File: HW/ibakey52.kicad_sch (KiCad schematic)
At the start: 55 parts, among them J1 AudioJack4, U1 Nice!Nano

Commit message: Renaming project
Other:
- sheet Keys: file ibakey54-keys.kicad_sch -> ibakey52-keys.kicad_sch

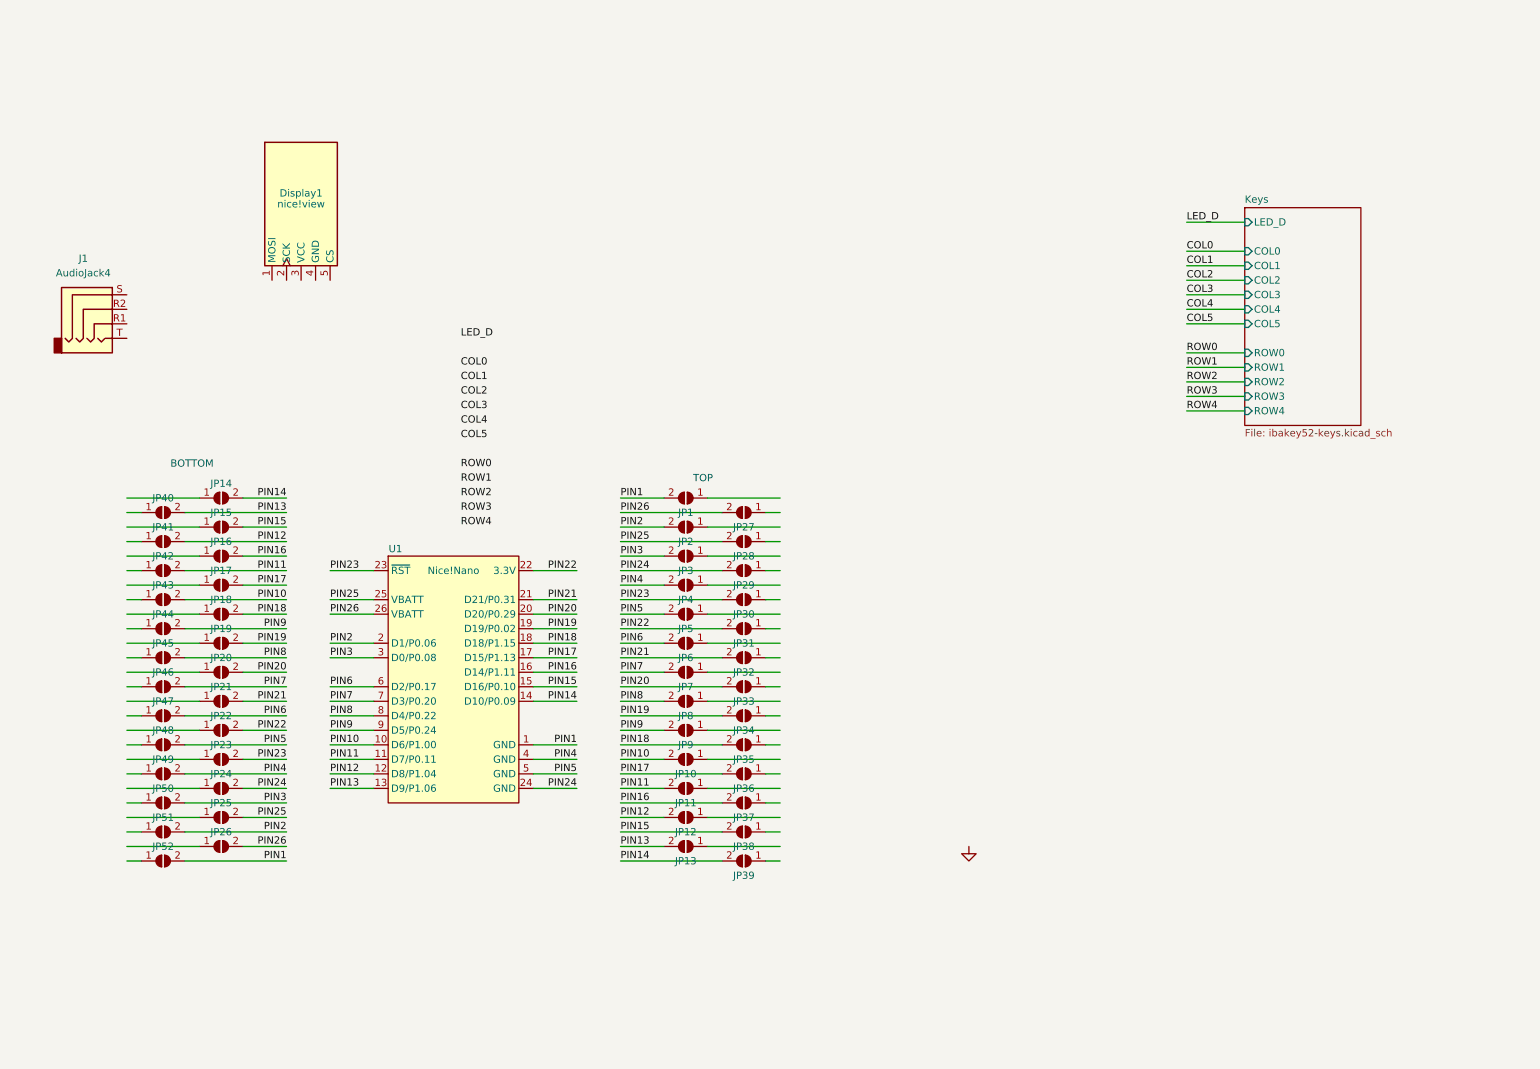
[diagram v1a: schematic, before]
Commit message: matrix routed
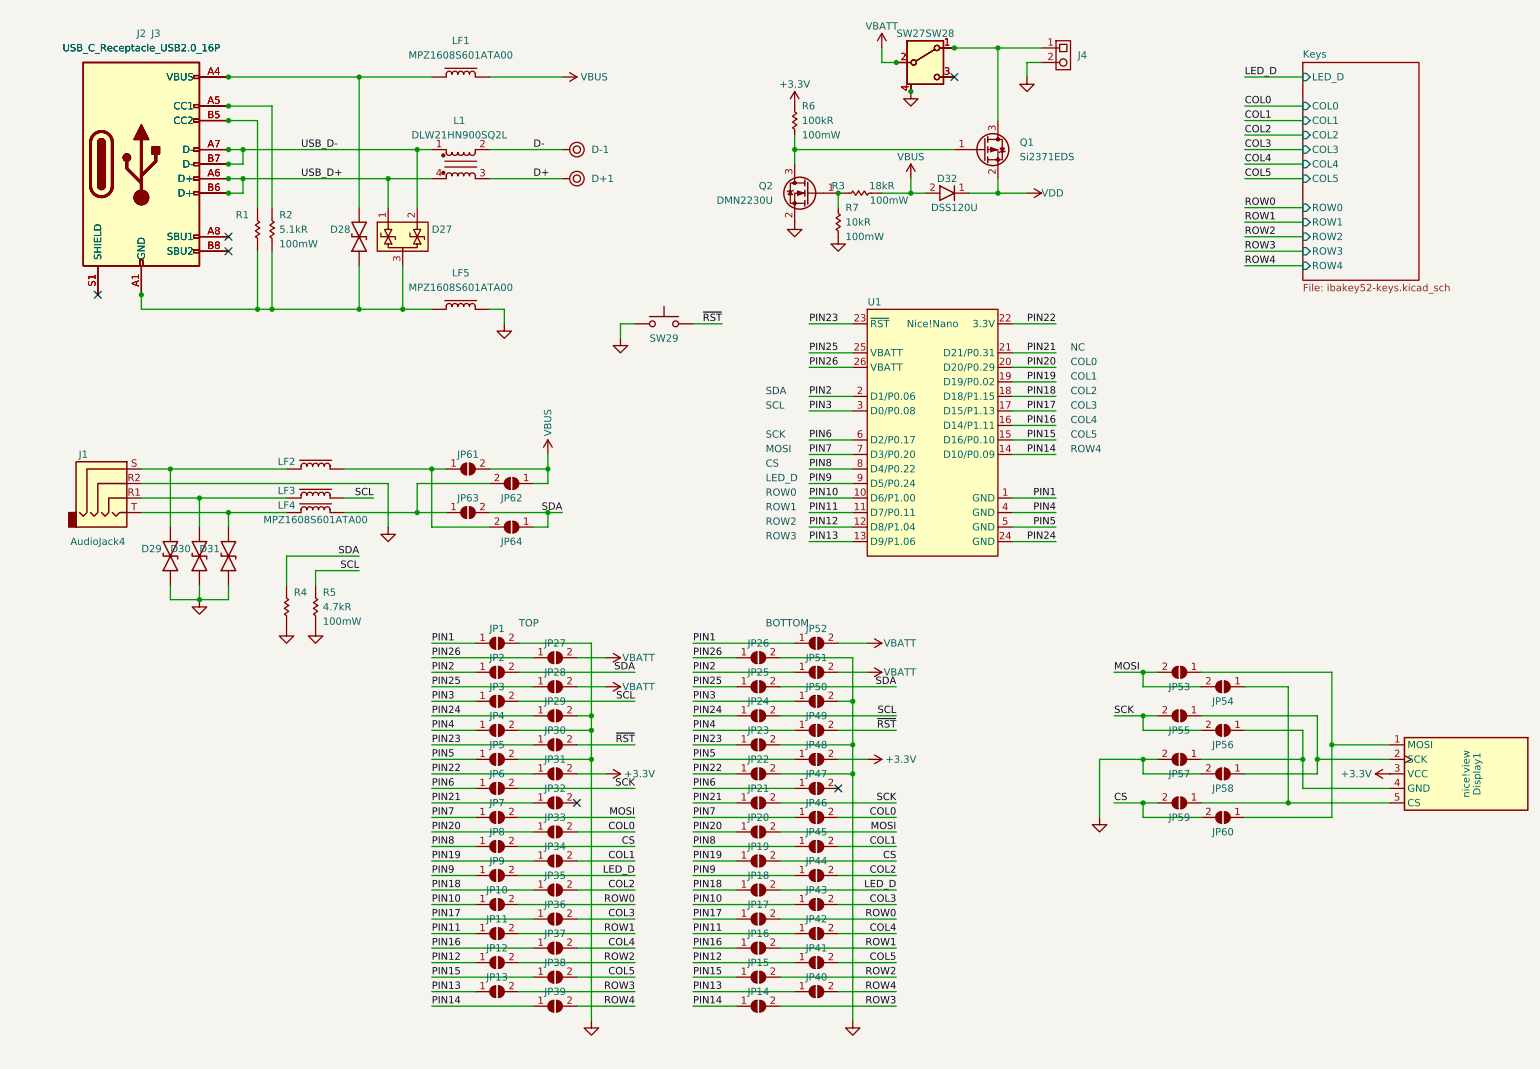
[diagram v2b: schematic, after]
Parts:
- added D+1, D-1: ~, WIRE-POINT:WP 20AWG, symbol WIRE-POINT:WP_22AWG
- added D27: D1213A-02WLQ-7, Package_TO_SOT_SMD:SOT-323_SC-70, symbol DIODE-SMD-TVS:D1213A-02WLQ-7
- added D28, D29, D30, D31: DESD5V0U1BA-7, Diode_SMD:D_SOD-323, symbol DIODE-SMD-TVS:DESD5V0U1BA-7
- added D32: DSS120U, Diode_SMD:D_SOD-123F, symbol DIODE-SMD-SCHOTTKY:DSS120U
- added J2, J3: USB_C_Receptacle_USB2.0_16P, CONN-USB:GCT_USB4520-03-0-A_REVA, symbol Connector:USB_C_Receptacle_USB2.0_16P
- added J4: ~, Connector_JST:JST_PH_S2B-PH-K_1x02_P2.00mm_Horizontal, symbol CONN-THT-HEADER:CONN-THT-1x2-P1.25-R
- added JP53, JP54, JP55, JP56, JP57, JP58, JP59, JP60, JP61, JP62, JP63, JP64: SolderJumper_2_Open, JUMPER:SJMP1.3mm, symbol Jumper:SolderJumper_2_Open
- added L1: DLW21HN900SQ2L, IND-SMD-CHOKE:FIL_DLW21HN900SQ2L, symbol IND-SMD-CHOKE:DLW21HN900SQ2L
- added LF1, LF2, LF3, LF4, LF5: MPZ1608S601ATA00, Inductor_SMD:L_0603_1608Metric, symbol FERRITE-SMD:MPZ1608S601ATA00
- added Q1: Si2371EDS, Package_TO_SOT_SMD:SOT-23, symbol Transistor_FET:Si2371EDS
- added Q2: DMN2230U, Package_TO_SOT_SMD:SOT-23, symbol Transistor_FET:DMN2230U
- added R1, R2: ${SIM.PARAMS}, Resistor_SMD:R_0603_1608Metric, symbol RES-SMD-100mW:5K1R-SMD-100mW-0603
- added R3: ${SIM.PARAMS}, Resistor_SMD:R_0603_1608Metric, symbol RES-SMD-100mW:18kR-SMD-100mW-0603
- added R4, R5: ${SIM.PARAMS}, Resistor_SMD:R_0603_1608Metric, symbol RES-SMD-100mW:4K7R-SMD-100mW-0603
- added R6: ${SIM.PARAMS}, Resistor_SMD:R_0603_1608Metric, symbol RES-SMD-100mW:100kR-SMD-100mW-0603
- added R7: ${SIM.PARAMS}, Resistor_SMD:R_0603_1608Metric, symbol RES-SMD-100mW:10kR-SMD-100mW-0603
- added SW27, SW28: SSSS811101, SWITCH-SMD-SLIDE:SSSS811101, symbol SWITCH-SMD-SLIDE:SSSS811101
- added SW29: SW_Push, SWITCH-SMD-PB:EVQ-PUL02K, symbol Switch:SW_Push
- JP1, JP10, JP11, JP12, JP13, JP14, JP15, JP16, JP17, JP18, JP19, JP2, JP20, JP21, JP22, JP23, JP24, JP25, JP26, JP27, JP28, JP29, JP3, JP30, JP31, JP32, JP33, JP34, JP35, JP36, JP37, JP38, JP39, JP4, JP40, JP41, JP42, JP43, JP44, JP45, JP46, JP47, JP48, JP49, JP5, JP50, JP51, JP52, JP6, JP7, JP8, JP9: footprint Jumper:SolderJumper-2_P1.3mm_Open_TrianglePad1.0x1.5mm -> JUMPER:SJMP1.3mm
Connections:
- net COL0: now also JP33.2 (B), JP46.2 (B)
- net COL1: now also JP34.2 (B), JP45.2 (B)
- net COL2: now also JP35.2 (B), JP44.2 (B)
- net COL3: now also JP36.2 (B), JP43.2 (B)
- net COL4: now also JP37.2 (B), JP42.2 (B)
- net COL5: now also JP38.2 (B), JP41.2 (B)
- net GND: now also J1.R2, JP1.2 (B), JP22.2 (B), JP23.2 (B), JP26.2 (B), JP29.2 (B), JP4.2 (B), JP5.2 (B), JP50.2 (B), D29.1 (A1), D30.1 (A1), D31.1 (A1), J4.2, JP57.2 (B), JP58.2 (B), LF5.2, Q2.2 (S), R4.2, R5.2, R7.2, SW27.4 (GND), SW28.4 (GND), SW29.1
- net LED_D: now also JP18.2 (B), JP9.2 (B)
- net PIN1: now also JP1.1 (A), JP52.1 (A); no longer JP1.2 (B), JP52.2 (B)
- net PIN10: now also JP10.1 (A), JP43.1 (A); no longer JP10.2 (B), JP43.2 (B)
- net PIN11: now also JP11.1 (A), JP42.1 (A); no longer JP11.2 (B), JP42.2 (B)
- net PIN12: now also JP12.1 (A), JP41.1 (A); no longer JP12.2 (B), JP41.2 (B)
- net PIN13: now also JP13.1 (A), JP40.1 (A); no longer JP13.2 (B), JP40.2 (B)
- net PIN14: now also JP14.1 (A), JP39.1 (A); no longer JP14.2 (B), JP39.2 (B)
- net PIN15: now also JP15.1 (A), JP38.1 (A); no longer JP15.2 (B), JP38.2 (B)
- net PIN16: now also JP16.1 (A), JP37.1 (A); no longer JP16.2 (B), JP37.2 (B)
- net PIN17: now also JP17.1 (A), JP36.1 (A); no longer JP17.2 (B), JP36.2 (B)
- net PIN18: now also JP18.1 (A), JP35.1 (A); no longer JP18.2 (B), JP35.2 (B)
- net PIN19: now also JP19.1 (A), JP34.1 (A); no longer JP19.2 (B), JP34.2 (B)
- net PIN2: now also JP2.1 (A), JP51.1 (A); no longer JP2.2 (B), JP51.2 (B)
- net PIN20: now also JP20.1 (A), JP33.1 (A); no longer JP20.2 (B), JP33.2 (B)
- net PIN21: now also JP21.1 (A), JP32.1 (A); no longer JP21.2 (B), JP32.2 (B)
- net PIN22: now also JP22.1 (A), JP31.1 (A); no longer JP22.2 (B), JP31.2 (B)
- net PIN23: now also JP23.1 (A), JP30.1 (A); no longer JP23.2 (B), JP30.2 (B)
- net PIN24: now also JP24.1 (A), JP29.1 (A); no longer JP24.2 (B), JP29.2 (B)
- net PIN25: now also JP25.1 (A), JP28.1 (A); no longer JP25.2 (B), JP28.2 (B)
- net PIN26: now also JP26.1 (A), JP27.1 (A); no longer JP26.2 (B), JP27.2 (B)
- net PIN3: now also JP3.1 (A), JP50.1 (A); no longer JP3.2 (B), JP50.2 (B)
- net PIN4: now also JP4.1 (A), JP49.1 (A); no longer JP4.2 (B), JP49.2 (B)
- net PIN5: now also JP48.1 (A), JP5.1 (A); no longer JP48.2 (B), JP5.2 (B)
- net PIN6: now also JP47.1 (A), JP6.1 (A); no longer JP47.2 (B), JP6.2 (B)
- net PIN7: now also JP46.1 (A), JP7.1 (A); no longer JP46.2 (B), JP7.2 (B)
- net PIN8: now also JP45.1 (A), JP8.1 (A); no longer JP45.2 (B), JP8.2 (B)
- net PIN9: now also JP44.1 (A), JP9.1 (A); no longer JP44.2 (B), JP9.2 (B)
- net ROW0: now also JP10.2 (B), JP17.2 (B)
- net ROW1: now also JP11.2 (B), JP16.2 (B)
- net ROW2: now also JP12.2 (B), JP15.2 (B)
- net ROW3: now also JP13.2 (B), JP14.2 (B)
- net ROW4: now also JP39.2 (B), JP40.2 (B)
- net at Display1.1 (MOSI): now also JP53.1 (A), JP60.1 (A)
- net at Display1.2 (SCK): now also JP55.1 (A), JP58.1 (A)
- net +3.3V: now reaches Display1.3 (VCC)
- net +3.3V: now also JP31.2 (B), JP48.2 (B), R6.1
- net at Display1.4 (GND): now also JP56.1 (A), JP57.1 (A)
- net at Display1.5 (CS): now also JP54.1 (A), JP59.1 (A)
- net at J1.R1: now also D30.2 (A2), LF3.1
- net at J1.S: now also D29.2 (A2), LF2.1
- net at J1.T: now also D31.2 (A2), LF4.1
- new net: Q2.1 (G), R3.1, R7.1
- new net: J2.A5 (CC1), J3.A5 (CC1), R2.1
- new net: D27.3 (common), D28.1 (A1), J2.A1 (GND), J2.A12 (GND), J2.B1 (GND), J2.B12 (GND), J3.A1 (GND), J3.A12 (GND), J3.B1 (GND), J3.B12 (GND), LF5.1, R1.2, R2.2
- new net: J4.1, Q1.3 (D), SW27.1 (A), SW28.1 (A)
- new net: SW27.3 (C), SW28.3 (C)
- new net: D28.2 (A2), J2.A4 (VBUS), J2.A9 (VBUS), J2.B4 (VBUS), J2.B9 (VBUS), J3.A4 (VBUS), J3.A9 (VBUS), J3.B4 (VBUS), J3.B9 (VBUS), LF1.1
- new net: J2.A8 (SBU1), J3.A8 (SBU1)
- new net: J2.B5 (CC2), J3.B5 (CC2), R1.1
- new net: J2.B8 (SBU2), J3.B8 (SBU2)
- new net: J2.S1 (SHIELD), J3.S1 (SHIELD)
- new net: JP62.2 (B), JP63.1 (A), LF4.2
- new net: JP61.1 (A), JP64.2 (B), LF2.2
- new net: Q1.1 (G), Q2.3 (D), R6.2
- new net CS: JP19.2 (B), JP59.2 (B), JP60.2 (B), JP8.2 (B)
- new net D+: D+1.1, L1.3
- new net D-: D-1.1, L1.2
- new net MOSI: JP20.2 (B), JP53.2 (B), JP54.2 (B), JP7.2 (B)
- new net SCK: JP21.2 (B), JP55.2 (B), JP56.2 (B), JP6.2 (B)
- new net SCL: JP24.2 (B), JP3.2 (B), LF3.2, R5.1
- new net SDA: JP2.2 (B), JP25.2 (B), JP63.2 (B), JP64.1 (A), R4.1
- new net USB_D+: D27.1 (A1), J2.A6 (D+), J2.B6 (D+), J3.A6 (D+), J3.B6 (D+), L1.4
- new net USB_D-: D27.2 (A2), J2.A7 (D-), J2.B7 (D-), J3.A7 (D-), J3.B7 (D-), L1.1
- new net VBATT: JP27.2 (B), JP28.2 (B), JP51.2 (B), JP52.2 (B), SW27.2 (B), SW28.2 (B)
- new net VBUS: D32.2 (A), JP61.2 (B), JP62.1 (A), LF1.2, R3.2
- new net VDD: D32.1 (K), Q1.2 (S)
- new net ~{RST}: JP30.2 (B), JP49.2 (B), SW29.2
- no-connect marks 0 -> 6
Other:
- note added: "COL0"
- note added: "COL1"
- note added: "COL2"
- note added: "COL3"
- note added: "COL4"
- note added: "COL5"
- note added: "CS"
- note added: "LED_D"
- note added: "MOSI"
- note added: "NC"
- note added: "ROW0"
- note added: "ROW1"
- note added: "ROW2"
- note added: "ROW3"
- note added: "ROW4"
- note added: "SCK"
- note added: "SCL"
- note added: "SDA"
- moved on the sheet: Display1, J1, JP1, JP10, JP11, JP12, JP13, JP14, JP15, JP16, JP17, JP18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

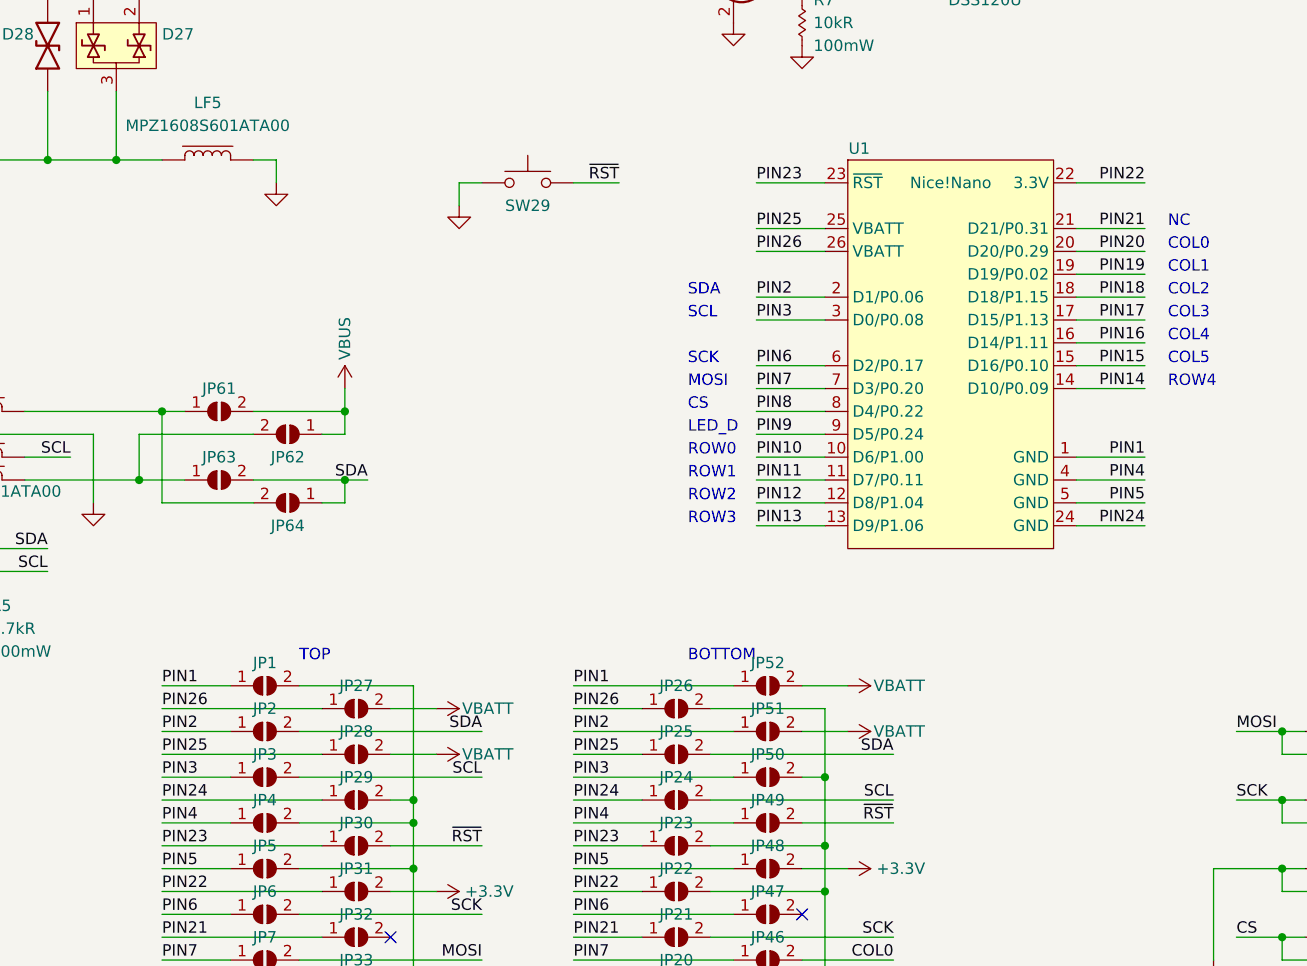
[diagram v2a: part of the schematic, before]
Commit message: correcting switch footprint & updating LED routing
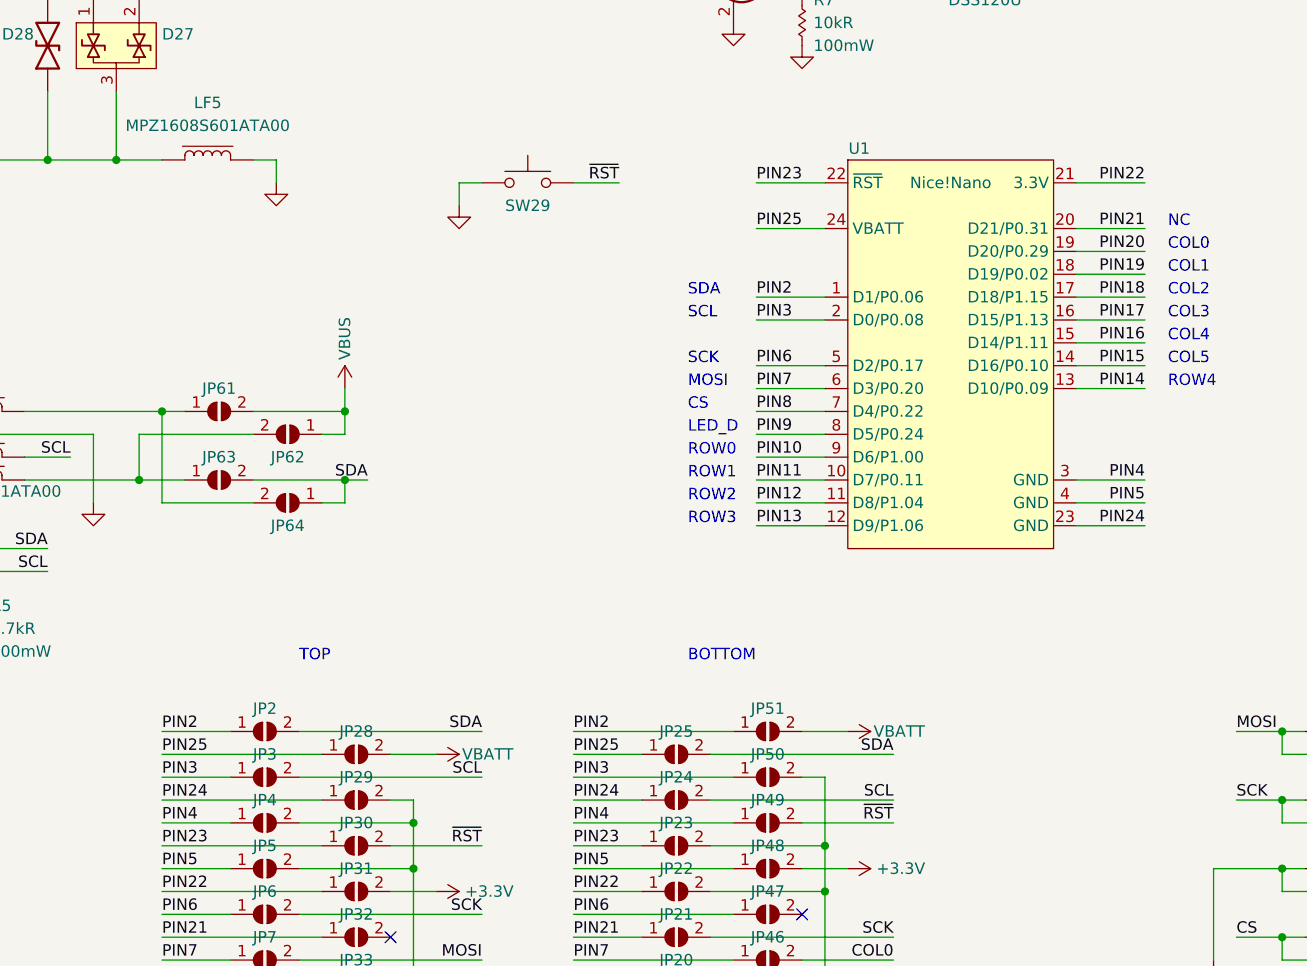
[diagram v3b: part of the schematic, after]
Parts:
- removed JP1, JP26, JP27, JP52: SolderJumper_2_Open, JUMPER:SJMP1.3mm, symbol Jumper:SolderJumper_2_Open
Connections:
- net PIN1 is gone; now on net PIN2: U1.1 (D1/P0.06)
- net PIN10: now also U1.9 (D6/P1.00); no longer U1.10 (D6/P1.00)
- net PIN11: now also U1.10 (D7/P0.11); no longer U1.11 (D7/P0.11)
- net PIN12: now also U1.11 (D8/P1.04); no longer U1.12 (D8/P1.04)
- net PIN13: now also U1.12 (D9/P1.06); no longer U1.13 (D9/P1.06)
- net PIN14: now also U1.13 (D10/P0.09); no longer U1.14 (D10/P0.09)
- net PIN15: now also U1.14 (D16/P0.10); no longer U1.15 (D16/P0.10)
- net PIN16: now also U1.15 (D14/P1.11); no longer U1.16 (D14/P1.11)
- net PIN17: now also U1.16 (D15/P1.13); no longer U1.17 (D15/P1.13)
- net PIN18: now also U1.17 (D18/P1.15); no longer U1.18 (D18/P1.15)
- net PIN19: now also U1.18 (D19/P0.02); no longer U1.19 (D19/P0.02)
- net PIN2: no longer U1.2 (D1/P0.06)
- net PIN20: now also U1.19 (D20/P0.29); no longer U1.20 (D20/P0.29)
- net PIN21: now also U1.20 (D21/P0.31); no longer U1.21 (D21/P0.31)
- net PIN22: now also U1.21 (3.3V); no longer U1.22 (3.3V)
- net PIN23: now also U1.22 (~{RST}); no longer U1.23 (~{RST})
- net PIN24: now also U1.23 (GND); no longer U1.24 (GND)
- net PIN25: now also U1.24 (VBATT); no longer U1.25 (VBATT)
- net PIN3: now also U1.2 (D0/P0.08); no longer U1.3 (D0/P0.08)
- net PIN4: now also U1.3 (GND); no longer U1.4 (GND)
- net PIN5: now also U1.4 (GND); no longer U1.5 (GND)
- net PIN6: now also U1.5 (D2/P0.17); no longer U1.6 (D2/P0.17)
- net PIN7: now also U1.6 (D3/P0.20); no longer U1.7 (D3/P0.20)
- net PIN8: now also U1.7 (D4/P0.22); no longer U1.8 (D4/P0.22)
- net PIN9: now also U1.8 (D5/P0.24); no longer U1.9 (D5/P0.24)
- net at D27.3 (common), D28.1 (A1), J2.A1 (GND)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: no longer J2.A12 (GND), J2.B12 (GND)
- net at D28.2 (A2), J2.A4 (VBUS), J2.B4 (VBUS)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: no longer J2.A9 (VBUS), J2.B9 (VBUS)
- removed net PIN26: U1.26 (VBATT)

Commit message: ibakey52v1.0
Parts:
- removed D+1, D-1: ~, WIRE-POINT:WP 20AWG, symbol WIRE-POINT:WP_22AWG
- removed D32: DSS120U, Diode_SMD:D_SOD-123F, symbol DIODE-SMD-SCHOTTKY:DSS120U
- removed Q1: Si2371EDS, Package_TO_SOT_SMD:SOT-23, symbol Transistor_FET:Si2371EDS
- removed Q2: DMN2230U, Package_TO_SOT_SMD:SOT-23, symbol Transistor_FET:DMN2230U
- removed R3: ${SIM.PARAMS}, Resistor_SMD:R_0603_1608Metric, symbol RES-SMD-100mW:18kR-SMD-100mW-0603
- removed R6: ${SIM.PARAMS}, Resistor_SMD:R_0603_1608Metric, symbol RES-SMD-100mW:100kR-SMD-100mW-0603
- removed R7: ${SIM.PARAMS}, Resistor_SMD:R_0603_1608Metric, symbol RES-SMD-100mW:10kR-SMD-100mW-0603
- added C53, C54: ${SIM.PARAMS}, Capacitor_SMD:C_0402_1005Metric, symbol CAP-SMD-25V:1uF-CER-25V-0603
- added J5: ~, CONN-EDGE:CONN-FLEX-IBAKEY, symbol CONN-EDGE:CONN-EDGE-IBA-FLEX
- added J6: ~, Connector_JST:JST_PH_S2B-PH-K_1x02_P2.00mm_Horizontal, symbol CONN-THT-HEADER:CONN-THT-1x2-P1.25-R
- added MH1, MH2, MH3, MH4, MH5, MH6: ~, MNTG-HOLE:M2-STANDOFF-PASS, symbol MNTG-HOLE:MNTG-HOLE
- added U2: TPS22917DBV, Package_TO_SOT_SMD:SOT-23-6, symbol Power_Management:TPS22917DBV
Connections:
- net +3.3V: now also C53.1, U2.1 (VIN)
- net D+: now also J5.2
- net D-: now also J5.3
- net GND: now also C53.2, C54.2, J5.4, J6.2, U2.2 (GND)
- net VBUS: now also J5.1
- net VDD: now also C54.1, U2.6 (VOUT)
- net at D27.3 (common), D28.1 (A1), J2.A1 (GND)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: no longer J3.A12 (GND), J3.B12 (GND)
- net at J4.1, SW27.1 (A), SW28.1 (A): now also J6.1
- net LED_EN: now reaches JP47.2 (B)
- net LED_EN: now also JP32.2 (B), U2.3 (ON)
- net at D28.2 (A2), J2.A4 (VBUS), J2.B4 (VBUS)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: no longer J3.A9 (VBUS), J3.B9 (VBUS)
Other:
- note added: "LED_EN"
- note removed: "NC"
- moved on the sheet: J4, SW27, SW28
